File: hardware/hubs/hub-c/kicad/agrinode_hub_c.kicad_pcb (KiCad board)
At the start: 2 copper layers, 130 x 96 mm, 119 parts, among them J1 DC 12V 5.5/2.1, J10 LTE MODULE, J2 DC IN 7-24V, J3 SOLAR 6-24V, J4 USB 5V / PROG, J5 BAT NTC 10k, J6 PROG, J7 I2C, J8 LED STRIP WS2813, J9 RS-485, Q1 AO3401A, Q2 AO3401A, Q3 MMBT3904, Q4 MMBT3904, Q5 BSS138, Q6 MMBT3904, Q7 AO3401A, Q8 MMBT3904, Q9 MMBT3904, SW1 RESET, SW2 BOOT / PAIR, U1 LM2596S-5.0, U2 TP4056, U3 MIC29302WU, U4 ESP32-WROOM-32E-N8, U5 CH340C, U6 DS3231MZ, U7 MAX3485ESA, U8 MIC29302WU

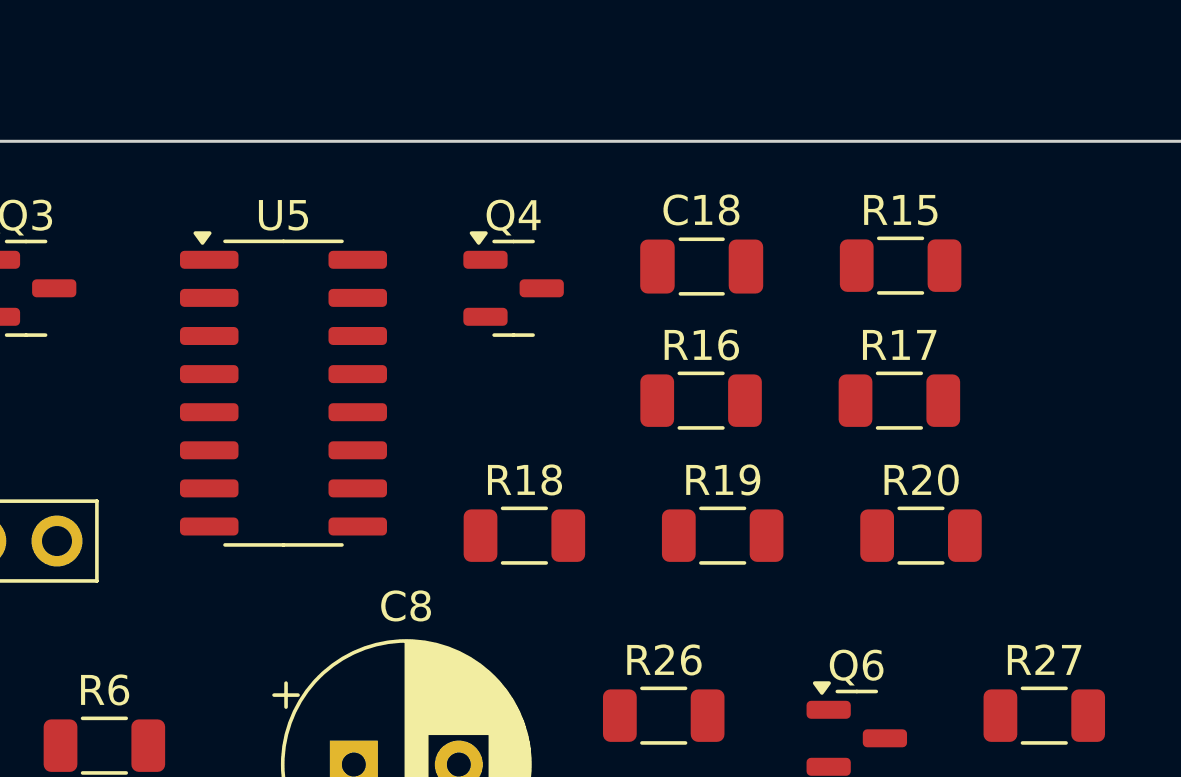
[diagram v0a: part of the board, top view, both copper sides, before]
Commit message: hubs: CH340C rotated so USB D+/D- face the USB-B jack; reroute in progress
Co-Authored-By: Claude Opus 5.5 <noreply@anthropic.com>
Claude-Session: https://claude.ai/code/session_014J7amXZ5Y6AZWEh5CjDNja
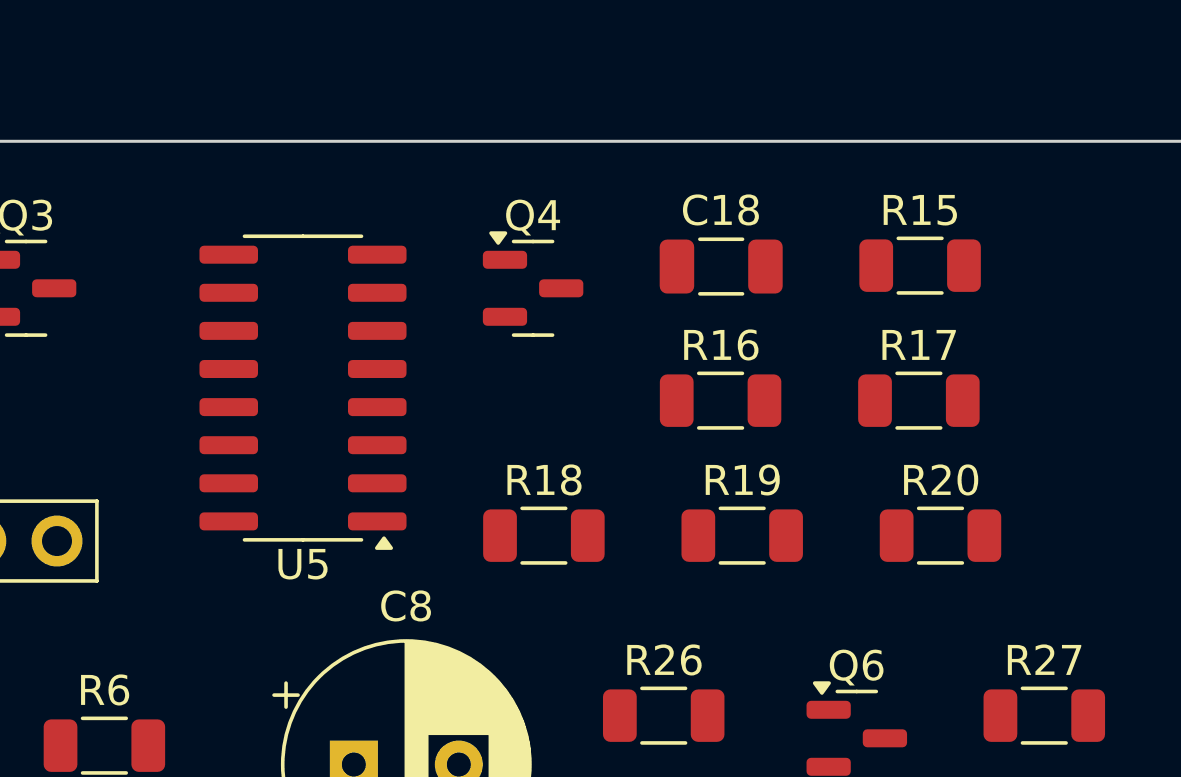
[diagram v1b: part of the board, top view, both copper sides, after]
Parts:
- moved U5 0.67 mm to (133.7, 58.2), turned to 180 degrees
- moved R18 0.65 mm to (141.8, 63.1)
- moved R19 0.65 mm to (148.4, 63.1)
- moved R20 0.65 mm to (155.0, 63.1)
- moved C18 0.65 mm to (147.7, 54.2)
- moved Q4 0.65 mm to (141.4, 54.9)
- moved R16 0.65 mm to (147.6, 58.6)
- moved R17 0.65 mm to (154.3, 58.6)
- moved R15 0.65 mm to (154.3, 54.1)

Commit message: hubs: routing progress snapshot
Co-Authored-By: Claude Opus 5.5 <noreply@anthropic.com>
Claude-Session: https://claude.ai/code/session_014J7amXZ5Y6AZWEh5CjDNja
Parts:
- moved R27 61.4 mm to (120.8, 117.6)
- moved R26 44.0 mm to (146.6, 113.1)
- moved R7 28.1 mm to (145.7, 67.6)
- moved R8 28.1 mm to (145.7, 72.1)
- moved R22 23.5 mm to (145.8, 94.1)
- moved C19 21.3 mm to (133.3, 113.2)
- moved U6 20.5 mm to (137.7, 95.7), turned to 180 degrees
- moved R21 14.8 mm to (140.0, 113.1)
- moved U7 13.6 mm to (137.7, 119.4)
- moved D9 13.5 mm to (158.4, 69.2)
- moved C21 10.5 mm to (145.8, 117.7)
- moved D10 4.50 mm to (146.8, 99.4)
- moved R28 2.80 mm to (145.8, 122.1)
- moved R30 1.13 mm to (127.4, 117.6)
- moved C10 1.00 mm to (136.8, 105.3)
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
